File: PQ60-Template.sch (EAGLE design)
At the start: 3 parts, among them X1-BOT FX8C-60S-SV, X1-TOP FX8C-60P-SV

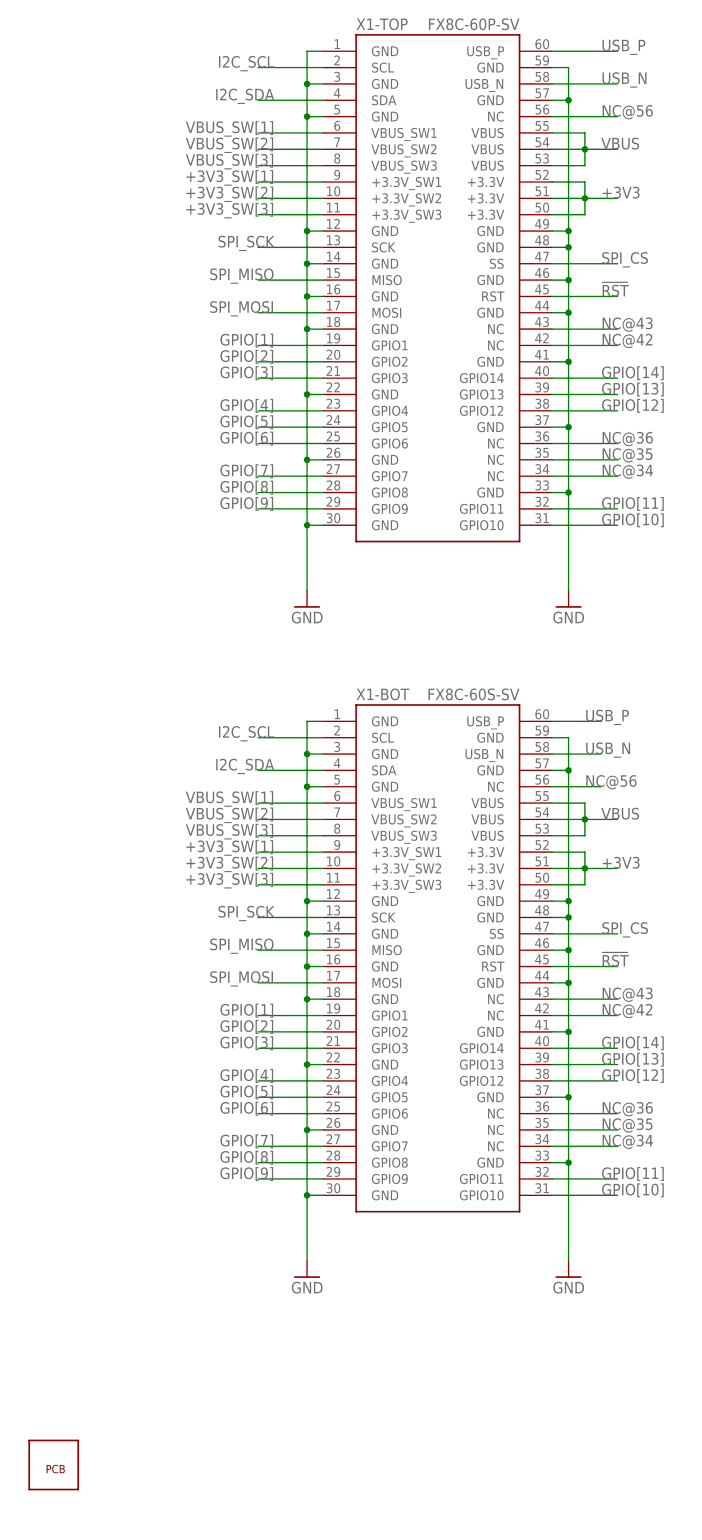
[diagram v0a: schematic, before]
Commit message: Update to new PQ60 v1.1 standard.
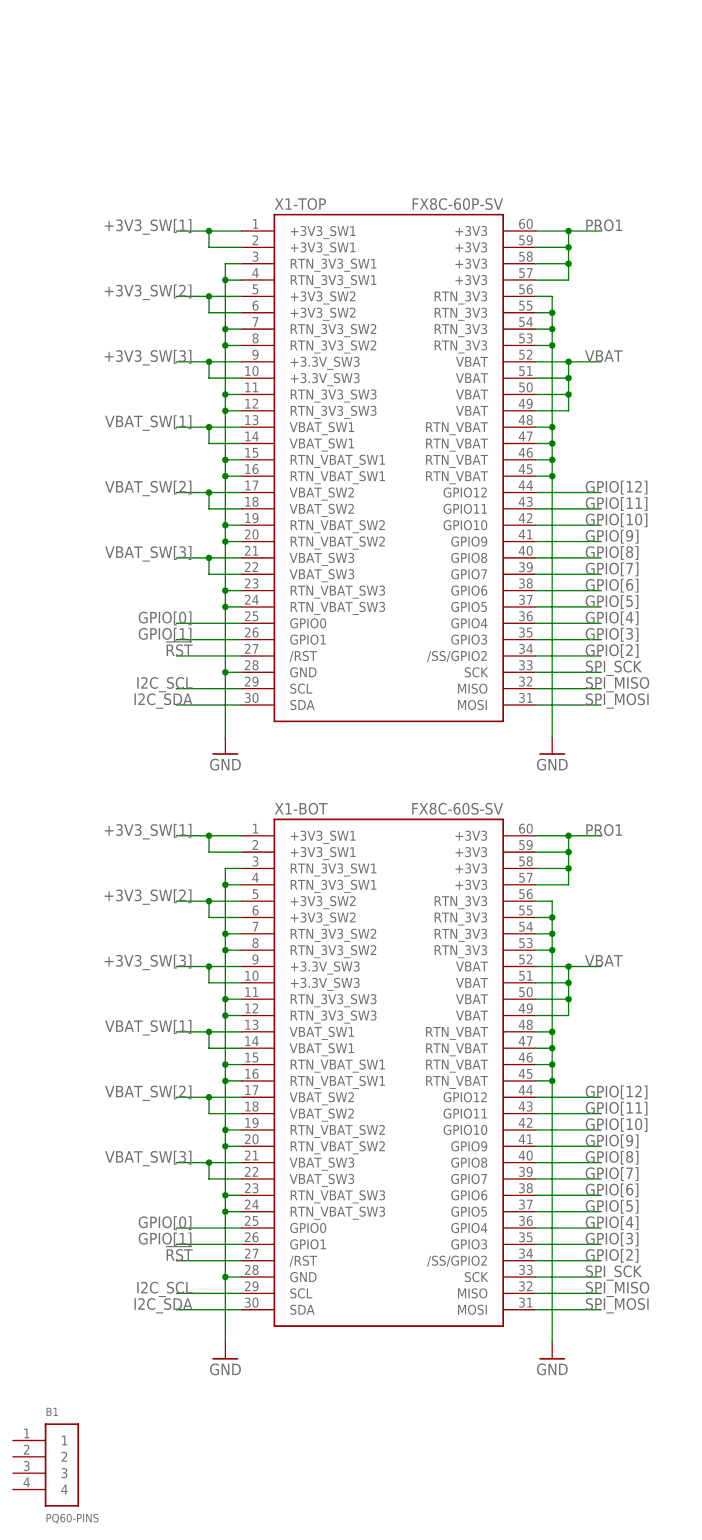
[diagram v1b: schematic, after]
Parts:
- B1: value PQ60-NOPINS -> PQ60-PINS; device general:PQ60-NOPINS -> general:PQ60-PINS; OC_FARNELL (none) -> unknown
- X1-BOT: device PQ60:FX8C-60S-SV -> PQ60:FX8C-60-R2S-SV; OC_FARNELL (none) -> unknown
- X1-TOP: device PQ60:FX8C-60P-SV -> PQ60:FX8C-60-R2P-SV; OC_FARNELL (none) -> unknown
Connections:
- removed net +3V3: X1-BOT.+3.3V@1, X1-BOT.+3.3V@2, X1-BOT.+3.3V@3, X1-TOP.+3.3V@1, X1-TOP.+3.3V@2, X1-TOP.+3.3V@3
- removed net GPIO[13]: X1-BOT.GPIO13, X1-TOP.GPIO13
- removed net GPIO[14]: X1-BOT.GPIO14, X1-TOP.GPIO14
- removed net NC@34: X1-BOT.NC@1, X1-TOP.NC@1
- removed net NC@35: X1-BOT.NC@2, X1-TOP.NC@2
- removed net NC@36: X1-BOT.NC@3, X1-TOP.NC@3
- removed net NC@42: X1-BOT.NC@5, X1-TOP.NC@5
- removed net NC@43: X1-BOT.NC@6, X1-TOP.NC@6
- removed net NC@56: X1-BOT.NC@7, X1-TOP.NC@7
- removed net SPI_CS: X1-BOT.SS, X1-TOP.SS
- removed net USB_N: X1-BOT.USB_N, X1-TOP.USB_N
- removed net USB_P: X1-BOT.USB_P, X1-TOP.USB_P
- removed net VBUS: X1-BOT.VBUS@1, X1-BOT.VBUS@2, X1-BOT.VBUS@3, X1-TOP.VBUS@1, X1-TOP.VBUS@2, X1-TOP.VBUS@3
- removed net VBUS_SW[1]: X1-BOT.VBUS_SW1, X1-TOP.VBUS_SW1
- removed net VBUS_SW[2]: X1-BOT.VBUS_SW2, X1-TOP.VBUS_SW2
- removed net VBUS_SW[3]: X1-BOT.VBUS_SW3, X1-TOP.VBUS_SW3
- new net GPIO[0]: X1-BOT.GPIO0@25, X1-TOP.GPIO0@25
- new net PRO1: X1-BOT.+3V3@57, X1-BOT.+3V3@58, X1-BOT.+3V3@59, X1-BOT.+3V3@60, X1-TOP.+3V3@57, X1-TOP.+3V3@58, X1-TOP.+3V3@59, X1-TOP.+3V3@60
- new net VBAT: X1-BOT.VBAT@49, X1-BOT.VBAT@50, X1-BOT.VBAT@51, X1-BOT.VBAT@52, X1-TOP.VBAT@49, X1-TOP.VBAT@50, X1-TOP.VBAT@51, X1-TOP.VBAT@52
- new net VBAT_SW[1]: X1-BOT.VBAT_SW1@13, X1-BOT.VBAT_SW1@14, X1-TOP.VBAT_SW1@13, X1-TOP.VBAT_SW1@14
- new net VBAT_SW[2]: X1-BOT.VBAT_SW2@17, X1-BOT.VBAT_SW2@18, X1-TOP.VBAT_SW2@17, X1-TOP.VBAT_SW2@18
- new net VBAT_SW[3]: X1-BOT.VBAT_SW3@21, X1-BOT.VBAT_SW3@22, X1-TOP.VBAT_SW3@21, X1-TOP.VBAT_SW3@22
- net !RST: now also X1-BOT./RST@27, X1-TOP./RST@27; no longer X1-BOT.RST, X1-TOP.RST
- net +3V3_SW[1]: now also X1-BOT.+3V3_SW1@1, X1-BOT.+3V3_SW1@2, X1-TOP.+3V3_SW1@1, X1-TOP.+3V3_SW1@2; no longer X1-BOT.+3.3V_SW1, X1-TOP.+3.3V_SW1
- net +3V3_SW[2]: now also X1-BOT.+3V3_SW2@5, X1-BOT.+3V3_SW2@6, X1-TOP.+3V3_SW2@5, X1-TOP.+3V3_SW2@6; no longer X1-BOT.+3.3V_SW2, X1-TOP.+3.3V_SW2
- net +3V3_SW[3]: now also X1-BOT.+3.3V_SW3@10, X1-BOT.+3.3V_SW3@9, X1-TOP.+3.3V_SW3@10, X1-TOP.+3.3V_SW3@9; no longer X1-BOT.+3.3V_SW3, X1-TOP.+3.3V_SW3
- net GND: now also X1-BOT.GND@28, X1-BOT.RTN_3V3@53, X1-BOT.RTN_3V3@54, X1-BOT.RTN_3V3@55, X1-BOT.RTN_3V3@56, X1-BOT.RTN_3V3_SW1@3, X1-BOT.RTN_3V3_SW1@4, X1-BOT.RTN_3V3_SW2@7, X1-BOT.RTN_3V3_SW2@8, X1-BOT.RTN_3V3_SW3@11, X1-BOT.RTN_3V3_SW3@12, X1-BOT.RTN_VBAT@45, X1-BOT.RTN_VBAT@46, X1-BOT.RTN_VBAT@47, X1-BOT.RTN_VBAT@48, X1-BOT.RTN_VBAT_SW1@15, X1-BOT.RTN_VBAT_SW1@16, X1-BOT.RTN_VBAT_SW2@19, X1-BOT.RTN_VBAT_SW2@20, X1-BOT.RTN_VBAT_SW3@23, X1-BOT.RTN_VBAT_SW3@24, X1-TOP.GND@28, X1-TOP.RTN_3V3@53, X1-TOP.RTN_3V3@54, X1-TOP.RTN_3V3@55, X1-TOP.RTN_3V3@56, X1-TOP.RTN_3V3_SW1@3, X1-TOP.RTN_3V3_SW1@4, X1-TOP.RTN_3V3_SW2@7, X1-TOP.RTN_3V3_SW2@8, X1-TOP.RTN_3V3_SW3@11, X1-TOP.RTN_3V3_SW3@12, X1-TOP.RTN_VBAT@45, X1-TOP.RTN_VBAT@46, X1-TOP.RTN_VBAT@47, X1-TOP.RTN_VBAT@48, X1-TOP.RTN_VBAT_SW1@15, X1-TOP.RTN_VBAT_SW1@16, X1-TOP.RTN_VBAT_SW2@19, X1-TOP.RTN_VBAT_SW2@20, X1-TOP.RTN_VBAT_SW3@23, X1-TOP.RTN_VBAT_SW3@24; no longer X1-BOT.GND@1, X1-BOT.GND@10, X1-BOT.GND@11, X1-BOT.GND@12, X1-BOT.GND@13, X1-BOT.GND@14, X1-BOT.GND@15, X1-BOT.GND@16, X1-BOT.GND@17, X1-BOT.GND@18, X1-BOT.GND@19, X1-BOT.GND@2, X1-BOT.GND@3, X1-BOT.GND@4, X1-BOT.GND@5, X1-BOT.GND@6, X1-BOT.GND@7, X1-BOT.GND@8, X1-BOT.GND@9, X1-TOP.GND@1, X1-TOP.GND@10, X1-TOP.GND@11, X1-TOP.GND@12, X1-TOP.GND@13, X1-TOP.GND@14, X1-TOP.GND@15, X1-TOP.GND@16, X1-TOP.GND@17, X1-TOP.GND@18, X1-TOP.GND@19, X1-TOP.GND@2, X1-TOP.GND@3, X1-TOP.GND@4, X1-TOP.GND@5, X1-TOP.GND@6, X1-TOP.GND@7, X1-TOP.GND@8, X1-TOP.GND@9
- net GPIO[10]: now also X1-BOT.GPIO10@42, X1-TOP.GPIO10@42; no longer X1-BOT.GPIO10, X1-TOP.GPIO10
- net GPIO[11]: now also X1-BOT.GPIO11@43, X1-TOP.GPIO11@43; no longer X1-BOT.GPIO11, X1-TOP.GPIO11
- net GPIO[12]: now also X1-BOT.GPIO12@44, X1-TOP.GPIO12@44; no longer X1-BOT.GPIO12, X1-TOP.GPIO12
- net GPIO[1]: now also X1-BOT.GPIO1@26, X1-TOP.GPIO1@26; no longer X1-BOT.GPIO1, X1-TOP.GPIO1
- net GPIO[2]: now also X1-BOT./SS/GPIO2@34, X1-TOP./SS/GPIO2@34; no longer X1-BOT.GPIO2, X1-TOP.GPIO2
- net GPIO[3]: now also X1-BOT.GPIO3@35, X1-TOP.GPIO3@35; no longer X1-BOT.GPIO3, X1-TOP.GPIO3
- net GPIO[4]: now also X1-BOT.GPIO4@36, X1-TOP.GPIO4@36; no longer X1-BOT.GPIO4, X1-TOP.GPIO4
- net GPIO[5]: now also X1-BOT.GPIO5@37, X1-TOP.GPIO5@37; no longer X1-BOT.GPIO5, X1-TOP.GPIO5
- net GPIO[6]: now also X1-BOT.GPIO6@38, X1-TOP.GPIO6@38; no longer X1-BOT.GPIO6, X1-TOP.GPIO6
- net GPIO[7]: now also X1-BOT.GPIO7@39, X1-TOP.GPIO7@39; no longer X1-BOT.GPIO7, X1-TOP.GPIO7
- net GPIO[8]: now also X1-BOT.GPIO8@40, X1-TOP.GPIO8@40; no longer X1-BOT.GPIO8, X1-TOP.GPIO8
- net GPIO[9]: now also X1-BOT.GPIO9@41, X1-TOP.GPIO9@41; no longer X1-BOT.GPIO9, X1-TOP.GPIO9
- net I2C_SCL: now also X1-BOT.SCL@29, X1-TOP.SCL@29; no longer X1-BOT.SCL, X1-TOP.SCL
- net I2C_SDA: now also X1-BOT.SDA@30, X1-TOP.SDA@30; no longer X1-BOT.SDA, X1-TOP.SDA
- net SPI_MISO: now also X1-BOT.MISO@32, X1-TOP.MISO@32; no longer X1-BOT.MISO, X1-TOP.MISO
- net SPI_MOSI: now also X1-BOT.MOSI@31, X1-TOP.MOSI@31; no longer X1-BOT.MOSI, X1-TOP.MOSI
- net SPI_SCK: now also X1-BOT.SCK@33, X1-TOP.SCK@33; no longer X1-BOT.SCK, X1-TOP.SCK
